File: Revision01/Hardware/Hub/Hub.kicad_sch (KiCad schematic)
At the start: 25 parts, among them J20 Conn_01x04, J3 Conn_01x04, J4 Conn_01x05, J5 Conn_01x05, SW1 ON/OFF_SW_SPST_LED, U1 NUCLEO-L476RG, U2 LMR51603XFDBVR

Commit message: . Moved / Renamed "Revision01" libraries to "Hub"
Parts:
- J20: footprint Revision01:Battery_PinHeader_1x04_P2.54mm_Vertical -> Hub:Battery_PinHeader_1x04_P2.54mm_Vertical
- J3: footprint Revision01:BatterySwitch_PinHeader_1x04_P2.54mm_Vertical -> Hub:BatterySwitch_PinHeader_1x04_P2.54mm_Vertical
- J4: footprint Revision01:SPIExtra_PinHeader_1x05_P2.54mm_Vertical -> Hub:SPIExtra_PinHeader_1x05_P2.54mm_Vertical
- J5: footprint Revision01:GND_PinHeader_1x05_P2.54mm_Vertical -> Hub:GND_PinHeader_1x05_P2.54mm_Vertical
- L1: footprint Revision01:LQH44PH151MPRL_IND_LQH44PN_PR_MUR-M -> Hub:LQH44PH151MPRL_IND_LQH44PN_PR_MUR-M
- N1: footprint Revision01:BATT_HOLDER_18650_4_CELL_LEADS -> Hub:BATT_HOLDER_18650_4_CELL_LEADS
- R1: footprint Revision01:ZeroOhmSwitch_R_0805_2012Metric_Pad1.20x1.40mm_HandSolder -> Hub:ZeroOhmSwitch_R_0805_2012Metric_Pad1.20x1.40mm_HandSolder; symbol Revision01:ZeroOhmSwitch_R_Small -> Hub:ZeroOhmSwitch_R_Small
- U1: footprint Revision01:MODULE_NUCLEO-L476RG -> Hub:MODULE_NUCLEO-L476RG; symbol Revision01:NUCLEO-L476RG -> Hub:NUCLEO-L476RG
- U2: footprint Revision01:LMR51603XFDBVR_DBV0006A-MFG-IPC_C -> Hub:LMR51603XFDBVR_DBV0006A-MFG-IPC_C; symbol Revision01:LMR51603XFDBVR -> Hub:LMR51603XFDBVR
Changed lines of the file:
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@@
 		)
 		(instances
-			(project "Revision01"
+			(project "Hub"
 				(path "/955cc99e-a129-42cf-abc7-aa99813fdb5f"
 					(reference "TP2")
@@
 		)
 		(instances
-			(project "Revision01"
+			(project "Hub"
 				(path "/955cc99e-a129-42cf-abc7-aa99813fdb5f"
 					(reference "#PWR03")
@@
 		)
 		(instances
-			(project "Revision01"
+			(project "Hub"
 				(path "/955cc99e-a129-42cf-abc7-aa99813fdb5f"
 					(reference "#PWR018")
@@
 		)
 		(instances
-			(project "Revision01"
+			(project "Hub"
 				(path "/955cc99e-a129-42cf-abc7-aa99813fdb5f"
 					(reference "R4")
@@
 		)
 		(instances
-			(project "Revision01"
+			(project "Hub"
 				(path "/955cc99e-a129-42cf-abc7-aa99813fdb5f"
 					(reference "C5")
@@
 	)
 	(symbol
-		(lib_id "Revision01:BCIT-Racing-Logo_20mm_8mm8")
+		(lib_id "Hub:BCIT-Racing-Logo_20mm_8mm8")
 		(at 355.6 259.08 0)
 		(unit 1)
@@
 			)
 		)
-		(property "Footprint" "Revision01:BatterySwitch_PinHeader_1x04_P2.54mm_Vertical"
+		(property "Footprint" "Hub:BatterySwitch_PinHeader_1x04_P2.54mm_Vertical"
 			(at 82.55 85.09 0)
 			(effects
@@
 		)
 		(instances
-			(project "Revision01"
+			(project "Hub"
 				(path "/955cc99e-a129-42cf-abc7-aa99813fdb5f"
 					(reference "#PWR015")
@@
 		)
 		(instances
-			(project "Revision01"
+			(project "Hub"
 				(path "/955cc99e-a129-42cf-abc7-aa99813fdb5f"
 					(reference "H4")
@@
 	)
 	(symbol
-		(lib_id "Revision01:NUCLEO-L476RG")
+		(lib_id "Hub:NUCLEO-L476RG")
 		(at 115.57 209.55 0)
 		(unit 2)
@@
 			)
 		)
-		(property "Footprint" "Revision01:MODULE_NUCLEO-L476RG"
+		(property "Footprint" "Hub:MODULE_NUCLEO-L476RG"
 			(at 115.57 209.55 0)
 			(effects
@@
 		)
 		(instances
-			(project "Revision01"
+			(project "Hub"
 				(path "/955cc99e-a129-42cf-abc7-aa99813fdb5f"
 					(reference "U1")
@@
 		)
 		(instances
-			(project "Revision01"
+			(project "Hub"
 				(path "/955cc99e-a129-42cf-abc7-aa99813fdb5f"
 					(reference "C3")
@@
 		)
 		(instances
-			(project "Revision01"
+			(project "Hub"
 				(path "/955cc99e-a129-42cf-abc7-aa99813fdb5f"
 					(reference "H2")
@@
 		)
 		(instances
-			(project "Revision01"
+			(project "Hub"
 				(path "/955cc99e-a129-42cf-abc7-aa99813fdb5f"
 					(reference "#PWR022")
@@
 			)
 		)
-		(property "Footprint" "Revision01:GND_PinHeader_1x05_P2.54mm_Vertical"
+		(property "Footprint" "Hub:GND_PinHeader_1x05_P2.54mm_Vertical"
 			(at 171.45 266.7 0)
 			(effects
@@
 		)
 		(instances
-			(project "Revision01"
+			(project "Hub"
 				(path "/955cc99e-a129-42cf-abc7-aa99813fdb5f"
 					(reference "J5")
@@
 		)
 		(instances
-			(project "Revision01"
+			(project "Hub"
 				(path "/955cc99e-a129-42cf-abc7-aa99813fdb5f"
 					(reference "#PWR01")
@@
 		)
 		(instances
-			(project "Revision01"
+			(project "Hub"
 				(path "/955cc99e-a129-42cf-abc7-aa99813fdb5f"
 					(reference "#FLG02")
@@
 			)
 		)
-		(property "Footprint" "Revision01:LQH44PH151MPRL_IND_LQH44PN_PR_MUR-M"
+		(property "Footprint" "Hub:LQH44PH151MPRL_IND_LQH44PN_PR_MUR-M"
 			(at 194.31 83.82 0)
 			(effects
@@
 		)
 		(instances
-			(project "Revision01"
+			(project "Hub"
 				(path "/955cc99e-a129-42cf-abc7-aa99813fdb5f"
 					(reference "L1")
@@
 	)
 	(symbol
-		(lib_id "Revision01:LMR51603XFDBVR")
+		(lib_id "Hub:LMR51603XFDBVR")
 		(at 142.24 78.74 0)
 		(unit 1)
@@
 			)
 		)
-		(property "Footprint" "Revision01:LMR51603XFDBVR_DBV0006A-MFG-IPC_C"
+		(property "Footprint" "Hub:LMR51603XFDBVR_DBV0006A-MFG-IPC_C"
 			(at 142.24 78.74 0)
 			(effects
@@
 	)
 	(symbol
-		(lib_id "Revision01:NUCLEO-L476RG")
+		(lib_id "Hub:NUCLEO-L476RG")
 		(at 115.57 151.13 0)
 		(unit 1)
@@
 			)
 		)
-		(property "Footprint" "Revision01:MODULE_NUCLEO-L476RG"
+		(property "Footprint" "Hub:MODULE_NUCLEO-L476RG"
 			(at 115.57 151.13 0)
 			(effects
@@
 		)
 		(instances
-			(project "Revision01"
+			(project "Hub"
 				(path "/955cc99e-a129-42cf-abc7-aa99813fdb5f"
 					(reference "U1")
@@
 		)
 		(instances
-			(project "Revision01"
+			(project "Hub"
 				(path "/955cc99e-a129-42cf-abc7-aa99813fdb5f"
 					(reference "R3")
@@
 		)
 		(instances
-			(project "Revision01"
+			(project "Hub"
 				(path "/955cc99e-a129-42cf-abc7-aa99813fdb5f"
 					(reference "#FLG04")
@@
 		)
 		(instances
-			(project "Revision01"
+			(project "Hub"
 				(path "/955cc99e-a129-42cf-abc7-aa99813fdb5f"
 					(reference "#FLG03")
@@
 	)
 	(symbol
-		(lib_id "Revision01:NUCLEO-L476RG")
+		(lib_id "Hub:NUCLEO-L476RG")
 		(at 152.4 267.97 0)
 		(unit 3)
@@
 			)
 		)
-		(property "Footprint" "Revision01:MODULE_NUCLEO-L476RG"
+		(property "Footprint" "Hub:MODULE_NUCLEO-L476RG"
 			(at 152.4 267.97 0)
 			(effects
@@
 		)
 		(instances
-			(project "Revision01"
+			(project "Hub"
 				(path "/955cc99e-a129-42cf-abc7-aa99813fdb5f"
 					(reference "#PWR013")
@@
 		)
 		(instances
-			(project "Revision01"
+			(project "Hub"
 				(path "/955cc99e-a129-42cf-abc7-aa99813fdb5f"
 					(reference "BT1")
@@
 		)
 		(instances
-			(project "Revision01"
+			(project "Hub"
 				(path "/955cc99e-a129-42cf-abc7-aa99813fdb5f"
 					(reference "#PWR021")
@@
 		)
 		(instances
-			(project "Revision01"
+			(project "Hub"
 				(path "/955cc99e-a129-42cf-abc7-aa99813fdb5f"
 					(reference "#PWR09")
@@
 		)
 		(instances
-			(project "Revision01"
+			(project "Hub"
 				(path "/955cc99e-a129-42cf-abc7-aa99813fdb5f"
 					(reference "#PWR052")
@@
 		)
 		(instances
-			(project "Revision01"
+			(project "Hub"
 				(path "/955cc99e-a129-42cf-abc7-aa99813fdb5f"
 					(reference "H3")
@@
 			)
 		)
-		(property "Footprint" "Revision01:BATT_HOLDER_18650_4_CELL_LEADS"
+		(property "Footprint" "Hub:BATT_HOLDER_18650_4_CELL_LEADS"
 			(at 46.99 53.34 0)
 			(effects
@@
 			)
 		)
-		(property "Footprint" "Revision01:SPIExtra_PinHeader_1x05_P2.54mm_Vertical"
+		(property "Footprint" "Hub:SPIExtra_PinHeader_1x05_P2.54mm_Vertical"
 			(at 144.78 266.7 0)
 			(effects
@@
 		)
 		(instances
-			(project "Revision01"
+			(project "Hub"
 				(path "/955cc99e-a129-42cf-abc7-aa99813fdb5f"
 					(reference "#PWR07")
@@
 		)
 		(instances
-			(project "Revision01"
+			(project "Hub"
 				(path "/955cc99e-a129-42cf-abc7-aa99813fdb5f"
 					(reference "TP4")
@@
 		)
 		(instances
-			(project "Revision01"
+			(project "Hub"
 				(path "/955cc99e-a129-42cf-abc7-aa99813fdb5f"
 					(reference "#PWR010")
@@
 	)
 	(symbol
-		(lib_id "Revision01:ZeroOhmSwitch_R_Small")
+		(lib_id "Hub:ZeroOhmSwitch_R_Small")
 		(at 118.11 66.04 90)
 		(unit 1)
@@
 			)
 		)
-		(property "Footprint" "Revision01:ZeroOhmSwitch_R_0805_2012Metric_Pad1.20x1.40mm_HandSolder"
+		(property "Footprint" "Hub:ZeroOhmSwitch_R_0805_2012Metric_Pad1.20x1.40mm_HandSolder"
 			(at 118.11 66.04 0)
 			(effects
@@
 		)
 		(instances
-			(project "Revision01"
+			(project "Hub"
 				(path "/955cc99e-a129-42cf-abc7-aa99813fdb5f"
 					(reference "R1")
@@
 		)
 		(instances
-			(project "Revision01"
+			(project "Hub"
 				(path "/955cc99e-a129-42cf-abc7-aa99813fdb5f"
 					(reference "#PWR05")
@@
 		)
 		(instances
-			(project "Revision01"
+			(project "Hub"
 				(path "/955cc99e-a129-42cf-abc7-aa99813fdb5f"
 					(reference "#PWR019")
@@
 		)
 		(instances
-			(project "Revision01"
+			(project "Hub"
 				(path "/955cc99e-a129-42cf-abc7-aa99813fdb5f"
 					(reference "#PWR02")
@@
 			)
 		)
-		(property "Footprint" "Revision01:Battery_PinHeader_1x04_P2.54mm_Vertical"
+		(property "Footprint" "Hub:Battery_PinHeader_1x04_P2.54mm_Vertical"
 			(at 44.45 85.09 0)
 			(effects
@@
 		)
 		(instances
-			(project "Revision01"
+			(project "Hub"
 				(path "/955cc99e-a129-42cf-abc7-aa99813fdb5f"
 					(reference "#FLG05")
@@
 		)
 		(instances
-			(project "Revision01"
+			(project "Hub"
 				(path "/955cc99e-a129-42cf-abc7-aa99813fdb5f"
 					(reference "#FLG01")
@@
 		)
 		(instances
-			(project "Revision01"
+			(project "Hub"
 				(path "/955cc99e-a129-42cf-abc7-aa99813fdb5f"
 					(reference "#PWR016")
@@
 		)
 		(instances
-			(project "Revision01"
+			(project "Hub"
 				(path "/955cc99e-a129-42cf-abc7-aa99813fdb5f"
 					(reference "#PWR014")
@@
 		)
 		(instances
-			(project "Revision01"
+			(project "Hub"
 				(path "/955cc99e-a129-42cf-abc7-aa99813fdb5f"
 					(reference "#PWR020")
@@
 		)
 		(instances
-			(project "Revision01"
+			(project "Hub"
 				(path "/955cc99e-a129-42cf-abc7-aa99813fdb5f"
 					(reference "#PWR012")
@@
 		)
 		(instances
-			(project "Revision01"
+			(project "Hub"
 				(path "/955cc99e-a129-42cf-abc7-aa99813fdb5f"
 					(reference "#PWR04")
@@
 		)
 		(instances
-			(project "Revision01"
+			(project "Hub"
 				(path "/955cc99e-a129-42cf-abc7-aa99813fdb5f"
 					(reference "#PWR011")
@@
 		)
 		(instances
-			(project "Revision01"
+			(project "Hub"
 				(path "/955cc99e-a129-42cf-abc7-aa99813fdb5f"
 					(reference "TP1")
@@
 		)
 		(instances
-			(project "Revision01"
+			(project "Hub"
 				(path "/955cc99e-a129-42cf-abc7-aa99813fdb5f"
 					(reference "C4")

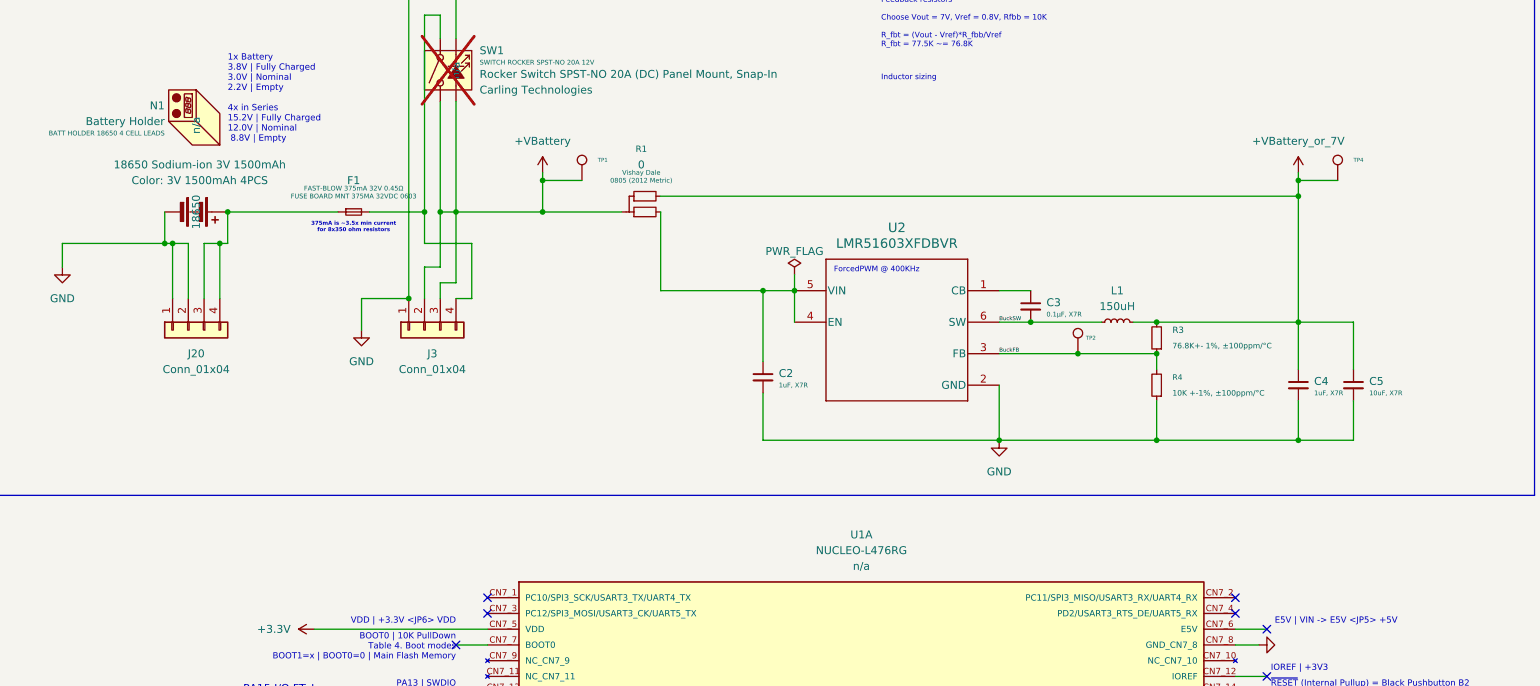
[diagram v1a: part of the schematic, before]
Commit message: . Split Hub symbol fields for Distributor Link/Part into DigiKey & AliExpress Link/Part in preparation for Mouser column.
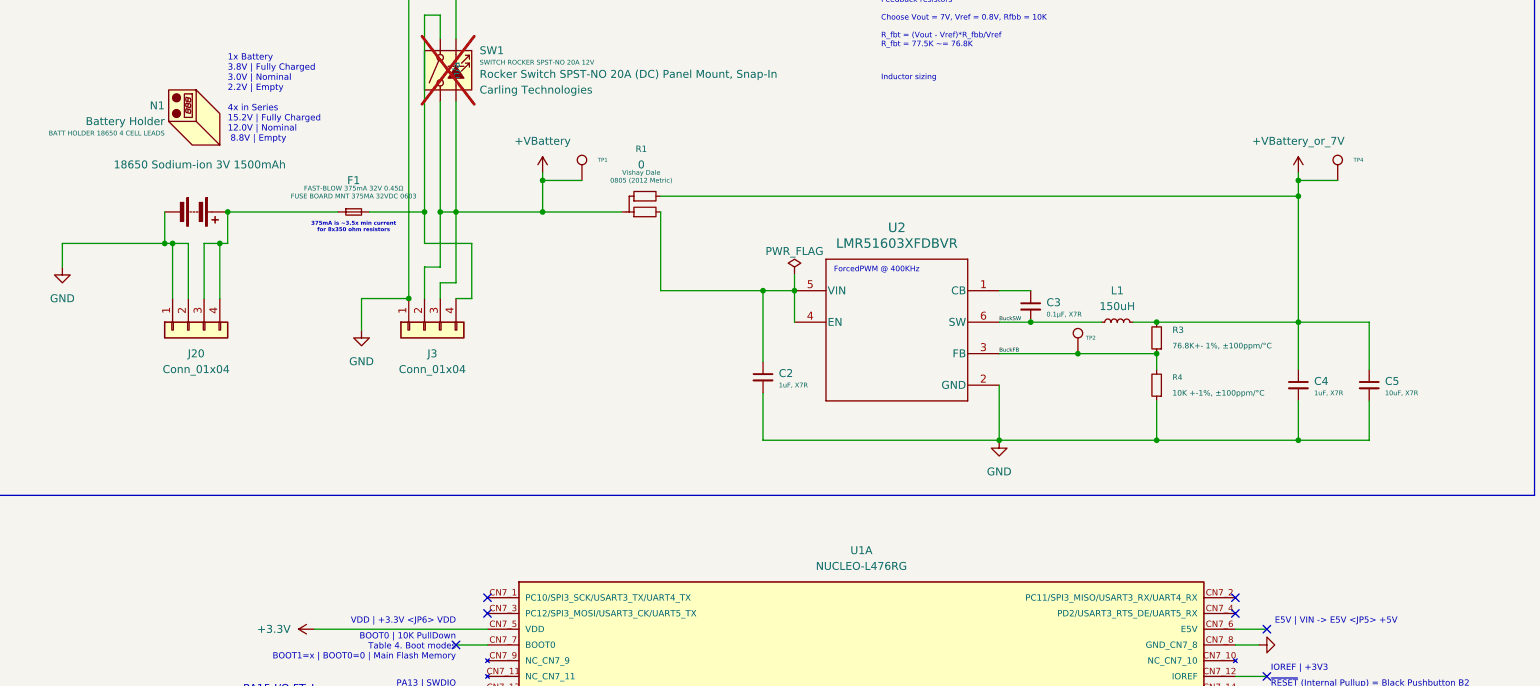
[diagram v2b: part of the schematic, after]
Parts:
- BT1: AliExpress Link (none) -> https://www.aliexpress.com/item/1005005859082063.html; AliExpress Part Number (none) -> Color: 3V 1500mAh 4PCS; DigiKey Link (none) -> https://www.aliexpress.com/item/1005005859082063.html; Distributor Link https://www.aliexpress.com/item/1005005859082063.html -> (none); Distributor Part Number Color: 3V 1500mAh 4PCS -> (none)
- C2, C4: DigiKey Link (none) -> https://www.digikey.ca/en/products/detail/samsung-electro-m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; DigiKey Part Number (none) -> 1276-1029-1-ND - Cut Tape (CT); Distributor Link https://www.digikey.ca/en/products/detail/samsung-electro-m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 -> (none); Distributor Part Number 1276-1029-1-ND - Cut Tape (CT) -> (none)
- C3: DigiKey Link (none) -> https://www.digikey.ca/en/products/detail/samsung-electro-m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; DigiKey Part Number (none) -> 1276-6840-1-ND - Cut Tape (CT); Distributor Link https://www.digikey.ca/en/products/detail/samsung-electro-m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 -> (none); Distributor Part Number 1276-6840-1-ND - Cut Tape (CT) -> (none)
- C5: DigiKey Link (none) -> https://www.digikey.ca/en/products/detail/samsung-electro-m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; DigiKey Part Number (none) -> 1276-1804-1-ND - Cut Tape (CT); Distributor Link https://www.digikey.ca/en/products/detail/samsung-electro-m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 -> (none); Distributor Part Number 1276-1804-1-ND - Cut Tape (CT) -> (none)
- F1: DigiKey Link (none) -> https://www.digikey.ca/en/products/detail/kyocera-avx/F0603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; DigiKey Part Number (none) -> 478-2859-1-ND - Cut Tape (CT); Distributor Link https://www.digikey.ca/en/products/detail/kyocera-avx/F0603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 -> (none); Distributor Part Number 478-2859-1-ND - Cut Tape (CT) -> (none)
- L1: DigiKey Link (none) -> https://www.digikey.com/en/products/detail/murata-electroni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; DigiKey Part Number (none) -> 490-LQH44PH151MPRLCT-ND - Cut Tape (CT); Distributor Link https://www.digikey.com/en/products/detail/murata-electroni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 -> (none); Distributor Part Number 490-LQH44PH151MPRLCT-ND - Cut Tape (CT) -> (none)
- N1: DigiKey Link (none) -> https://www.digikey.com/en/products/detail/seeed-technology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; DigiKey Part Number (none) -> 1597-114090052-ND; Distributor Link https://www.digikey.com/en/products/detail/seeed-technology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 -> (none); Distributor Part Number 1597-114090052-ND -> (none)
- R1: DigiKey Link (none) -> https://www.digikey.com/en/products/detail/vishay-dale/CRCW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; DigiKey Part Number (none) -> 541-0.0TBCT-ND - Cut Tape (CT); Distributor Link https://www.digikey.com/en/products/detail/vishay-dale/CRCW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 -> (none); Distributor Part Number 541-0.0TBCT-ND - Cut Tape (CT) -> (none)
- R3: DigiKey Link (none) -> https://www.digikey.com/en/products/detail/vishay-dale/CRCW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; DigiKey Part Number (none) -> 541-76.8KCCT-ND - Cut Tape (CT); Distributor Link https://www.digikey.com/en/products/detail/vishay-dale/CRCW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 -> (none); Distributor Part Number 541-76.8KCCT-ND - Cut Tape (CT) -> (none)
- R4: DigiKey Link (none) -> https://www.digikey.com/en/products/detail/vishay-dale/CRCW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; DigiKey Part Number (none) -> 541-3976-1-ND - Cut Tape (CT); Distributor Link https://www.digikey.com/en/products/detail/vishay-dale/CRCW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 -> (none); Distributor Part Number 541-3976-1-ND - Cut Tape (CT) -> (none)
- SW1: DigiKey Link (none) -> https://www.digikey.ca/en/products/detail/carling-technolog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; DigiKey Part Number (none) -> 432-V2D2S00B-GZCAD-100-XACT1-ND; Distributor Link https://www.digikey.ca/en/products/detail/carling-technolog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 -> (none); Distributor Part Number 432-V2D2S00B-GZCAD-100-XACT1-ND -> (none)
- U1: DigiKey Link (none) -> https://www.digikey.ca/en/products/detail/stmicroelectronic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; DigiKey Part Number (none) -> 497-15881-ND; Distributor Link https://www.digikey.ca/en/products/detail/stmicroelectronic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 -> (none); Distributor Part Number 497-15881-ND -> (none)
- U2: DigiKey Link (none) -> https://www.digikey.ca/en/products/detail/texas-instruments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; DigiKey Part Number (none) -> 296-LMR51606XDBVRCT-ND - Cut Tape (CT); Distributor Link https://www.digikey.ca/en/products/detail/texas-instruments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 -> (none); Distributor Part Number 296-LMR51606XDBVRCT-ND - Cut Tape (CT) -> (none)
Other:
- moved on the sheet: C5

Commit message: . Merged Amplifier & Hub libraries into "Lib" . Added Amplifier 6 pin IDC footprint . Finalized Amplifier layout & silkscreen
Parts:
- J20: footprint Hub:Battery_PinHeader_1x04_P2.54mm_Vertical -> Lib:Battery_PinHeader_1x04_P2.54mm_Vertical
- J3: footprint Hub:BatterySwitch_PinHeader_1x04_P2.54mm_Vertical -> Lib:BatterySwitch_PinHeader_1x04_P2.54mm_Vertical
- J4: footprint Hub:SPIExtra_PinHeader_1x05_P2.54mm_Vertical -> Lib:SPIExtra_PinHeader_1x05_P2.54mm_Vertical
- J5: footprint Hub:GND_PinHeader_1x05_P2.54mm_Vertical -> Lib:GND_PinHeader_1x05_P2.54mm_Vertical
- L1: footprint Hub:LQH44PH151MPRL_IND_LQH44PN_PR_MUR-M -> Lib:LQH44PH151MPRL_IND_LQH44PN_PR_MUR-M
- N1: footprint Hub:BATT_HOLDER_18650_4_CELL_LEADS -> Lib:BATT_HOLDER_18650_4_CELL_LEADS
- R1: footprint Hub:ZeroOhmSwitch_R_0805_2012Metric_Pad1.20x1.40mm_HandSolder -> Lib:ZeroOhmSwitch_R_0805_2012Metric_Pad1.20x1.40mm_HandSolder; symbol Hub:ZeroOhmSwitch_R_Small -> Lib:ZeroOhmSwitch_R_Small
- U1: footprint Hub:MODULE_NUCLEO-L476RG -> Lib:MODULE_NUCLEO-L476RG; symbol Hub:NUCLEO-L476RG -> Lib:NUCLEO-L476RG
- U2: footprint Hub:LMR51603XFDBVR_DBV0006A-MFG-IPC_C -> Lib:LMR51603XFDBVR_DBV0006A-MFG-IPC_C; symbol Hub:LMR51603XFDBVR -> Lib:LMR51603XFDBVR
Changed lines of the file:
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@@
 	)
 	(symbol
-		(lib_id "Hub:BCIT-Racing-Logo_20mm_8mm8")
+		(lib_id "Lib:BCIT-Racing-Logo_20mm_8mm8")
 		(at 355.6 259.08 0)
 		(unit 1)
@@
 			)
 		)
-		(property "Footprint" "Hub:BatterySwitch_PinHeader_1x04_P2.54mm_Vertical"
+		(property "Footprint" "Lib:BatterySwitch_PinHeader_1x04_P2.54mm_Vertical"
 			(at 82.55 85.09 0)
 			(effects
@@
 	)
 	(symbol
-		(lib_id "Hub:NUCLEO-L476RG")
+		(lib_id "Lib:NUCLEO-L476RG")
 		(at 115.57 209.55 0)
 		(unit 2)
@@
 			)
 		)
-		(property "Footprint" "Hub:MODULE_NUCLEO-L476RG"
+		(property "Footprint" "Lib:MODULE_NUCLEO-L476RG"
 			(at 115.57 209.55 0)
 			(effects
@@
 			)
 		)
-		(property "Footprint" "Hub:GND_PinHeader_1x05_P2.54mm_Vertical"
+		(property "Footprint" "Lib:GND_PinHeader_1x05_P2.54mm_Vertical"
 			(at 171.45 266.7 0)
 			(effects
@@
 			)
 		)
-		(property "Footprint" "Hub:LQH44PH151MPRL_IND_LQH44PN_PR_MUR-M"
+		(property "Footprint" "Lib:LQH44PH151MPRL_IND_LQH44PN_PR_MUR-M"
 			(at 194.31 83.82 0)
 			(effects
@@
 	)
 	(symbol
-		(lib_id "Hub:LMR51603XFDBVR")
+		(lib_id "Lib:LMR51603XFDBVR")
 		(at 142.24 78.74 0)
 		(unit 1)
@@
 			)
 		)
-		(property "Footprint" "Hub:LMR51603XFDBVR_DBV0006A-MFG-IPC_C"
+		(property "Footprint" "Lib:LMR51603XFDBVR_DBV0006A-MFG-IPC_C"
 			(at 142.24 78.74 0)
 			(effects
@@
 	)
 	(symbol
-		(lib_id "Hub:NUCLEO-L476RG")
+		(lib_id "Lib:NUCLEO-L476RG")
 		(at 115.57 151.13 0)
 		(unit 1)
@@
 			)
 		)
-		(property "Footprint" "Hub:MODULE_NUCLEO-L476RG"
+		(property "Footprint" "Lib:MODULE_NUCLEO-L476RG"
 			(at 115.57 151.13 0)
 			(effects
@@
 	)
 	(symbol
-		(lib_id "Hub:NUCLEO-L476RG")
+		(lib_id "Lib:NUCLEO-L476RG")
 		(at 152.4 267.97 0)
 		(unit 3)
@@
 			)
 		)
-		(property "Footprint" "Hub:MODULE_NUCLEO-L476RG"
+		(property "Footprint" "Lib:MODULE_NUCLEO-L476RG"
 			(at 152.4 267.97 0)
 			(effects
@@
 			)
 		)
-		(property "Footprint" "Hub:BATT_HOLDER_18650_4_CELL_LEADS"
+		(property "Footprint" "Lib:BATT_HOLDER_18650_4_CELL_LEADS"
 			(at 46.99 53.34 0)
 			(effects
@@
 			)
 		)
-		(property "Footprint" "Hub:SPIExtra_PinHeader_1x05_P2.54mm_Vertical"
+		(property "Footprint" "Lib:SPIExtra_PinHeader_1x05_P2.54mm_Vertical"
 			(at 144.78 266.7 0)
 			(effects
@@
 	)
 	(symbol
-		(lib_id "Hub:ZeroOhmSwitch_R_Small")
+		(lib_id "Lib:ZeroOhmSwitch_R_Small")
 		(at 118.11 66.04 90)
 		(unit 1)
@@
 			)
 		)
-		(property "Footprint" "Hub:ZeroOhmSwitch_R_0805_2012Metric_Pad1.20x1.40mm_HandSolder"
+		(property "Footprint" "Lib:ZeroOhmSwitch_R_0805_2012Metric_Pad1.20x1.40mm_HandSolder"
 			(at 118.11 66.04 0)
 			(effects
@@
 			)
 		)
-		(property "Footprint" "Hub:Battery_PinHeader_1x04_P2.54mm_Vertical"
+		(property "Footprint" "Lib:Battery_PinHeader_1x04_P2.54mm_Vertical"
 			(at 44.45 85.09 0)
 			(effects
